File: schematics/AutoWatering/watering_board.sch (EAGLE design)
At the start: 9 parts, among them IC2 REG1117, Q1 NMOSFET, Q2 NMOSFET

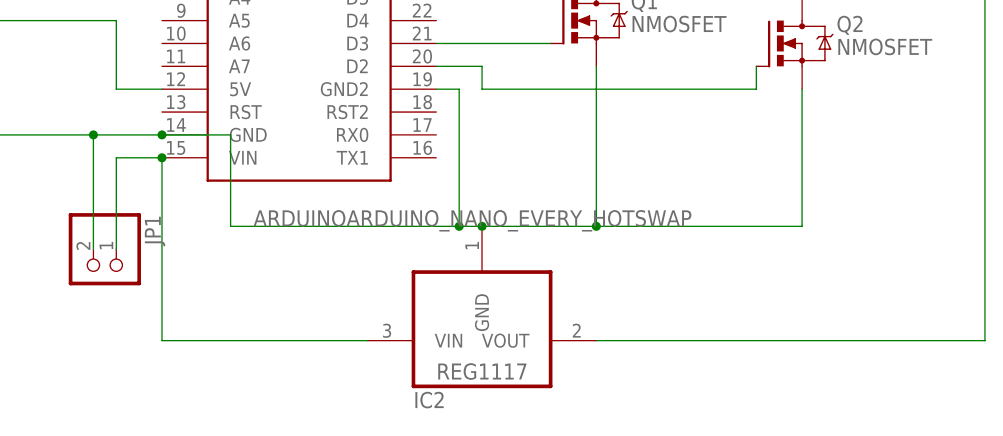
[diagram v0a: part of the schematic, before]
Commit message: Add missing LSO capacitors
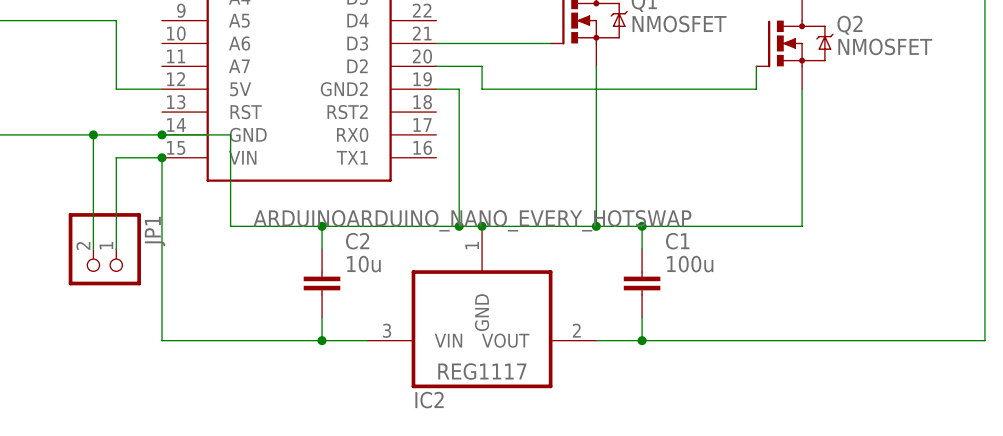
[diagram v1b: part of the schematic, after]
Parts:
- added C1: 100u, Capacitor:C_CHIP-1206(3216-METRIC)
- added C2: 10u, Capacitor:C_CHIP-1206(3216-METRIC)
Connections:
- net GND: now also C1.1, C2.1
- net N$4: now also C2.2
- net N$9: now also C1.2
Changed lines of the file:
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@@
 <part name="JP3" library="pinhead" library_urn="urn:adsk.eagle:library:325" deviceset="PINHD-1X2" device="" package3d_urn="urn:adsk.eagle:package:22435/2"/>
 <part name="IC2" library="burr-brown" library_urn="urn:adsk.eagle:library:111" deviceset="REG1117" device="" package3d_urn="urn:adsk.eagle:package:4940/1"/>
+<part name="C1" library="Capacitor" library_urn="urn:adsk.eagle:library:16290819" deviceset="C" device="CHIP-1206(3216-METRIC)" package3d_urn="urn:adsk.eagle:package:16290893/2" technology="_" value="100u"/>
+<part name="C2" library="Capacitor" library_urn="urn:adsk.eagle:library:16290819" deviceset="C" device="CHIP-1206(3216-METRIC)" package3d_urn="urn:adsk.eagle:package:16290893/2" technology="_" value="10u"/>
 </parts>
 <sheets>
@@
 <attribute name="NAME" x="68.58" y="6.985" size="1.778" layer="95" ratio="10" rot="MR180"/>
 <attribute name="VALUE" x="71.12" y="10.16" size="1.778" layer="96" ratio="10" rot="MR180"/>
+</instance>
+<instance part="C1" gate="G$1" x="93.98" y="20.32" smashed="yes">
+<attribute name="NAME" x="96.52" y="22.86" size="1.778" layer="95"/>
+<attribute name="VALUE" x="96.52" y="20.32" size="1.778" layer="96"/>
+</instance>
+<instance part="C2" gate="G$1" x="58.42" y="20.32" smashed="yes">
+<attribute name="NAME" x="60.96" y="22.86" size="1.778" layer="95"/>
+<attribute name="VALUE" x="60.96" y="20.32" size="1.778" layer="96"/>
 </instance>
 </instances>
@@
 <junction x="40.64" y="35.56"/>
 <wire x1="48.26" y1="35.56" x2="48.26" y2="25.4" width="0.1524" layer="91"/>
-<wire x1="48.26" y1="25.4" x2="73.66" y2="25.4" width="0.1524" layer="91"/>
+<wire x1="48.26" y1="25.4" x2="58.42" y2="25.4" width="0.1524" layer="91"/>
 <pinref part="Q2" gate="G$1" pin="S"/>
+<wire x1="58.42" y1="25.4" x2="73.66" y2="25.4" width="0.1524" layer="91"/>
 <wire x1="73.66" y1="25.4" x2="76.2" y2="25.4" width="0.1524" layer="91"/>
 <wire x1="76.2" y1="25.4" x2="88.9" y2="25.4" width="0.1524" layer="91"/>
-<wire x1="88.9" y1="25.4" x2="111.76" y2="25.4" width="0.1524" layer="91"/>
+<wire x1="88.9" y1="25.4" x2="93.98" y2="25.4" width="0.1524" layer="91"/>
+<wire x1="93.98" y1="25.4" x2="111.76" y2="25.4" width="0.1524" layer="91"/>
 <wire x1="111.76" y1="40.64" x2="111.76" y2="25.4" width="0.1524" layer="91"/>
 <pinref part="IC2" gate="G$1" pin="GND"/>
@@
 <wire x1="73.66" y1="40.64" x2="73.66" y2="25.4" width="0.1524" layer="91"/>
 <junction x="73.66" y="25.4"/>
+<pinref part="C2" gate="G$1" pin="1"/>
+<wire x1="58.42" y1="22.86" x2="58.42" y2="25.4" width="0.1524" layer="91"/>
+<junction x="58.42" y="25.4"/>
+<pinref part="C1" gate="G$1" pin="1"/>
+<wire x1="93.98" y1="22.86" x2="93.98" y2="25.4" width="0.1524" layer="91"/>
+<junction x="93.98" y="25.4"/>
 </segment>
 </net>
@@
 <junction x="40.64" y="33.02"/>
 <pinref part="IC2" gate="G$1" pin="VIN"/>
-<wire x1="40.64" y1="12.7" x2="63.5" y2="12.7" width="0.1524" layer="91"/>
+<wire x1="40.64" y1="12.7" x2="58.42" y2="12.7" width="0.1524" layer="91"/>
+<pinref part="C2" gate="G$1" pin="2"/>
+<wire x1="58.42" y1="12.7" x2="63.5" y2="12.7" width="0.1524" layer="91"/>
+<wire x1="58.42" y1="15.24" x2="58.42" y2="12.7" width="0.1524" layer="91"/>
+<junction x="58.42" y="12.7"/>
 </segment>
 </net>
@@
 <segment>
 <pinref part="IC2" gate="G$1" pin="VOUT"/>
-<wire x1="88.9" y1="12.7" x2="132.08" y2="12.7" width="0.1524" layer="91"/>
+<wire x1="88.9" y1="12.7" x2="93.98" y2="12.7" width="0.1524" layer="91"/>
+<wire x1="93.98" y1="12.7" x2="132.08" y2="12.7" width="0.1524" layer="91"/>
 <wire x1="132.08" y1="12.7" x2="132.08" y2="88.9" width="0.1524" layer="91"/>
 <wire x1="132.08" y1="88.9" x2="109.22" y2="88.9" width="0.1524" layer="91"/>
@@
 <wire x1="109.22" y1="78.74" x2="109.22" y2="88.9" width="0.1524" layer="91"/>
 <junction x="109.22" y="88.9"/>
+<pinref part="C1" gate="G$1" pin="2"/>
+<wire x1="93.98" y1="15.24" x2="93.98" y2="12.7" width="0.1524" layer="91"/>
+<junction x="93.98" y="12.7"/>
 </segment>
 </net>
@@
 packages will not be understood (or retained) with this version.
 </note>
+<note version="8.4" severity="warning">
+Since Version 8.4, EAGLE supports properties for SPICE simulation.
+Probes in schematics and SPICE mapping objects found in parts and library devices
+will not be understood with this version. Update EAGLE to the latest version
+for full support of SPICE simulation.
+</note>
 </compatibility>

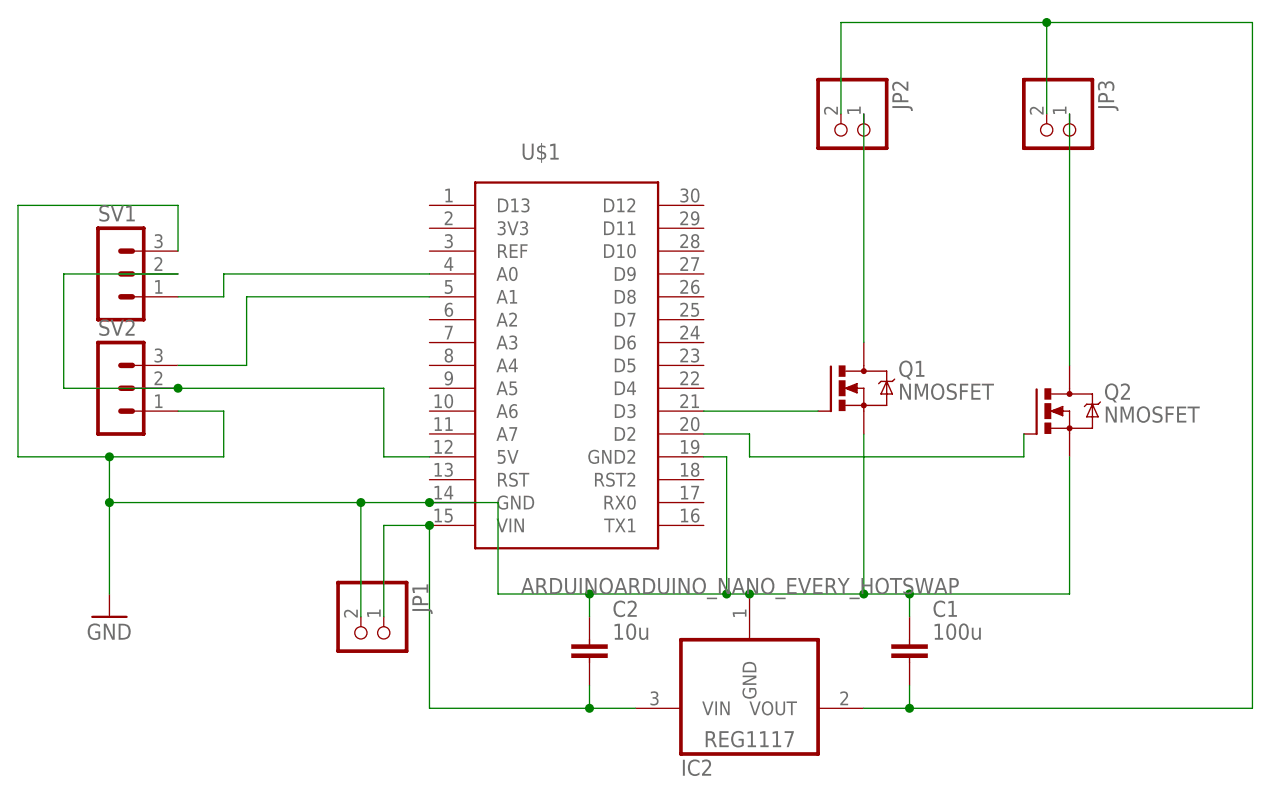
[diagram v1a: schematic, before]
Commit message: Use USB A conntector for the pump
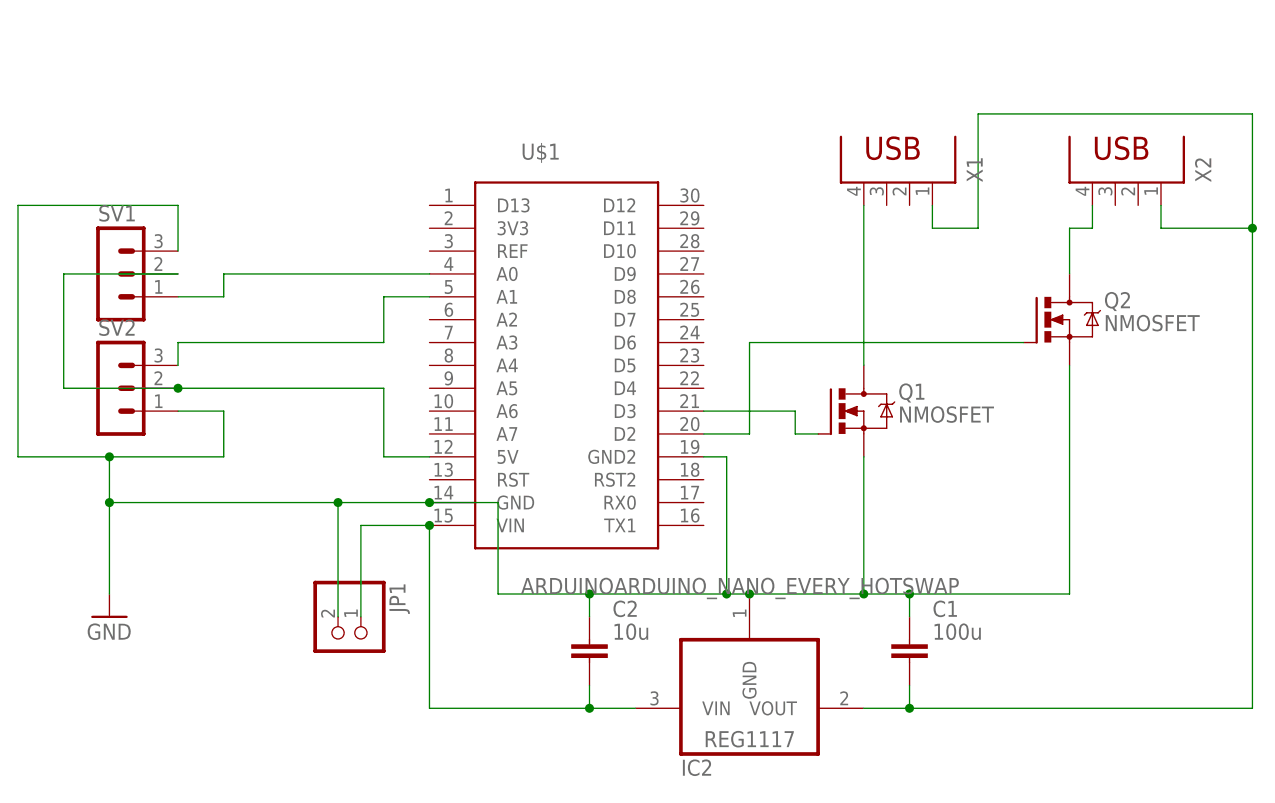
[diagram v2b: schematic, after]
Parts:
- removed JP2, JP3: (no value), pinhead:PINHD-1X2
- added X1, X2: (no value), con-berg:PN87520
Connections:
- net N$6: now also X1.4; no longer JP2.1
- net N$7: now also X2.4; no longer JP3.1
- net N$9: now also X1.1, X2.1; no longer JP2.2, JP3.2
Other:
- moved on the sheet: JP1, Q1, Q2

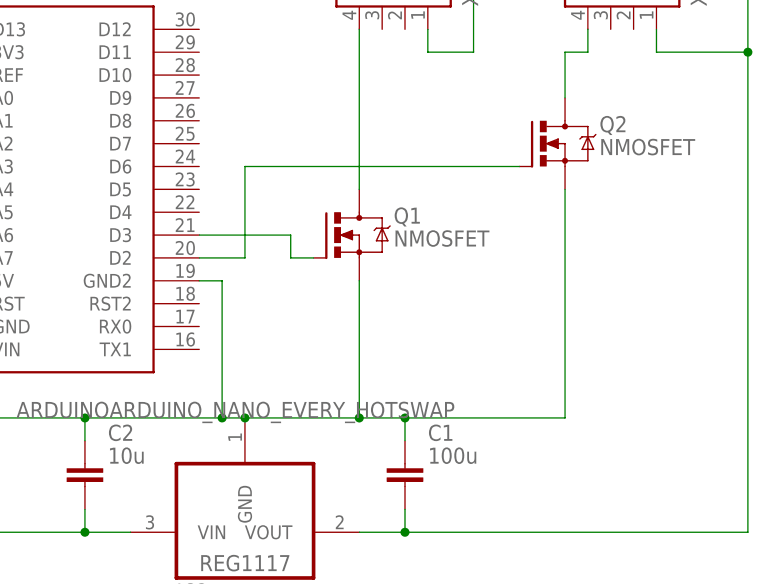
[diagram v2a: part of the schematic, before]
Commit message: Add the case
Add the case for the schematics.
Update to Arduino every. Use the difference sleep/wakeup mechnism.
Adjust moisture sensors.
Update schematics to match the case.
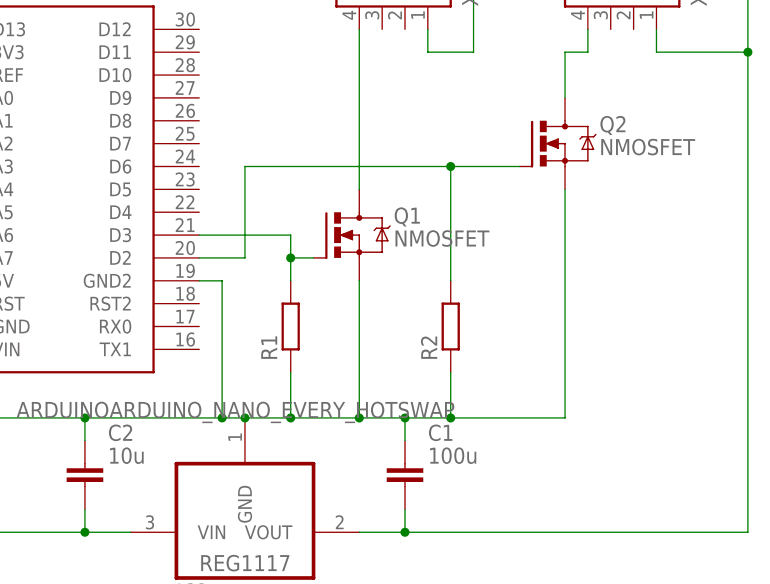
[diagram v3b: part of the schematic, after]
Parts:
- added R1, R2: (no value), rcl:R-EU_M1206
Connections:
- net GND: now also R1.1, R2.1
- net N$5: now also R2.2
- net N$8: now also R1.2
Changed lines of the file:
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@@
 <part name="X1" library="con-berg" library_urn="urn:adsk.eagle:library:130" deviceset="PN87520" device="" package3d_urn="urn:adsk.eagle:package:6146/1"/>
 <part name="X2" library="con-berg" library_urn="urn:adsk.eagle:library:130" deviceset="PN87520" device="" package3d_urn="urn:adsk.eagle:package:6146/1"/>
+<part name="R1" library="rcl" library_urn="urn:adsk.eagle:library:334" deviceset="R-EU_" device="M1206" package3d_urn="urn:adsk.eagle:package:23566/2"/>
+<part name="R2" library="rcl" library_urn="urn:adsk.eagle:library:334" deviceset="R-EU_" device="M1206" package3d_urn="urn:adsk.eagle:package:23566/2"/>
 </parts>
 <sheets>
@@
 <attribute name="NAME" x="125.73" y="71.12" size="1.778" layer="95" rot="MR90"/>
 <attribute name="VALUE" x="109.22" y="71.12" size="1.778" layer="96" rot="MR90"/>
+</instance>
+<instance part="R1" gate="G$1" x="81.28" y="35.56" smashed="yes" rot="R90">
+<attribute name="NAME" x="79.7814" y="31.75" size="1.778" layer="95" rot="R90"/>
+<attribute name="VALUE" x="84.582" y="31.75" size="1.778" layer="96" rot="R90"/>
+</instance>
+<instance part="R2" gate="G$1" x="99.06" y="35.56" smashed="yes" rot="R90">
+<attribute name="NAME" x="97.5614" y="31.75" size="1.778" layer="95" rot="R90"/>
+<attribute name="VALUE" x="102.362" y="31.75" size="1.778" layer="96" rot="R90"/>
 </instance>
 </instances>
@@
 <wire x1="58.42" y1="25.4" x2="73.66" y2="25.4" width="0.1524" layer="91"/>
 <wire x1="73.66" y1="25.4" x2="76.2" y2="25.4" width="0.1524" layer="91"/>
-<wire x1="76.2" y1="25.4" x2="88.9" y2="25.4" width="0.1524" layer="91"/>
+<wire x1="76.2" y1="25.4" x2="81.28" y2="25.4" width="0.1524" layer="91"/>
+<wire x1="81.28" y1="25.4" x2="88.9" y2="25.4" width="0.1524" layer="91"/>
 <wire x1="88.9" y1="25.4" x2="93.98" y2="25.4" width="0.1524" layer="91"/>
-<wire x1="93.98" y1="25.4" x2="111.76" y2="25.4" width="0.1524" layer="91"/>
+<wire x1="93.98" y1="25.4" x2="99.06" y2="25.4" width="0.1524" layer="91"/>
+<wire x1="99.06" y1="25.4" x2="111.76" y2="25.4" width="0.1524" layer="91"/>
 <wire x1="111.76" y1="50.8" x2="111.76" y2="25.4" width="0.1524" layer="91"/>
 <pinref part="IC2" gate="G$1" pin="GND"/>
@@
 <wire x1="93.98" y1="22.86" x2="93.98" y2="25.4" width="0.1524" layer="91"/>
 <junction x="93.98" y="25.4"/>
+<pinref part="R1" gate="G$1" pin="1"/>
+<wire x1="81.28" y1="30.48" x2="81.28" y2="25.4" width="0.1524" layer="91"/>
+<junction x="81.28" y="25.4"/>
+<pinref part="R2" gate="G$1" pin="1"/>
+<wire x1="99.06" y1="30.48" x2="99.06" y2="25.4" width="0.1524" layer="91"/>
+<junction x="99.06" y="25.4"/>
 </segment>
 </net>
@@
 <segment>
 <pinref part="Q2" gate="G$1" pin="G"/>
-<wire x1="76.2" y1="53.34" x2="106.68" y2="53.34" width="0.1524" layer="91"/>
+<wire x1="76.2" y1="53.34" x2="99.06" y2="53.34" width="0.1524" layer="91"/>
+<wire x1="99.06" y1="53.34" x2="106.68" y2="53.34" width="0.1524" layer="91"/>
 <wire x1="76.2" y1="53.34" x2="76.2" y2="43.18" width="0.1524" layer="91"/>
 <pinref part="U$1" gate="G$1" pin="D2"/>
 <wire x1="76.2" y1="43.18" x2="71.12" y2="43.18" width="0.1524" layer="91"/>
+<pinref part="R2" gate="G$1" pin="2"/>
+<wire x1="99.06" y1="40.64" x2="99.06" y2="53.34" width="0.1524" layer="91"/>
+<junction x="99.06" y="53.34"/>
 </segment>
 </net>
@@
 <wire x1="81.28" y1="45.72" x2="81.28" y2="43.18" width="0.1524" layer="91"/>
 <wire x1="81.28" y1="43.18" x2="83.82" y2="43.18" width="0.1524" layer="91"/>
-</segment>
-</net>
+<pinref part="R1" gate="G$1" pin="2"/>
+<wire x1="81.28" y1="40.64" x2="81.28" y2="43.18" width="0.1524" layer="91"/>
+<junction x="81.28" y="43.18"/>
+</segment>
+</net>
